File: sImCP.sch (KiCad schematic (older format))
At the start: 79 parts, among them J1 AVR-ISP-6, SW1 RESET, SW2 BOOT, U1 ATmega328P-AU, Y1 16MHz

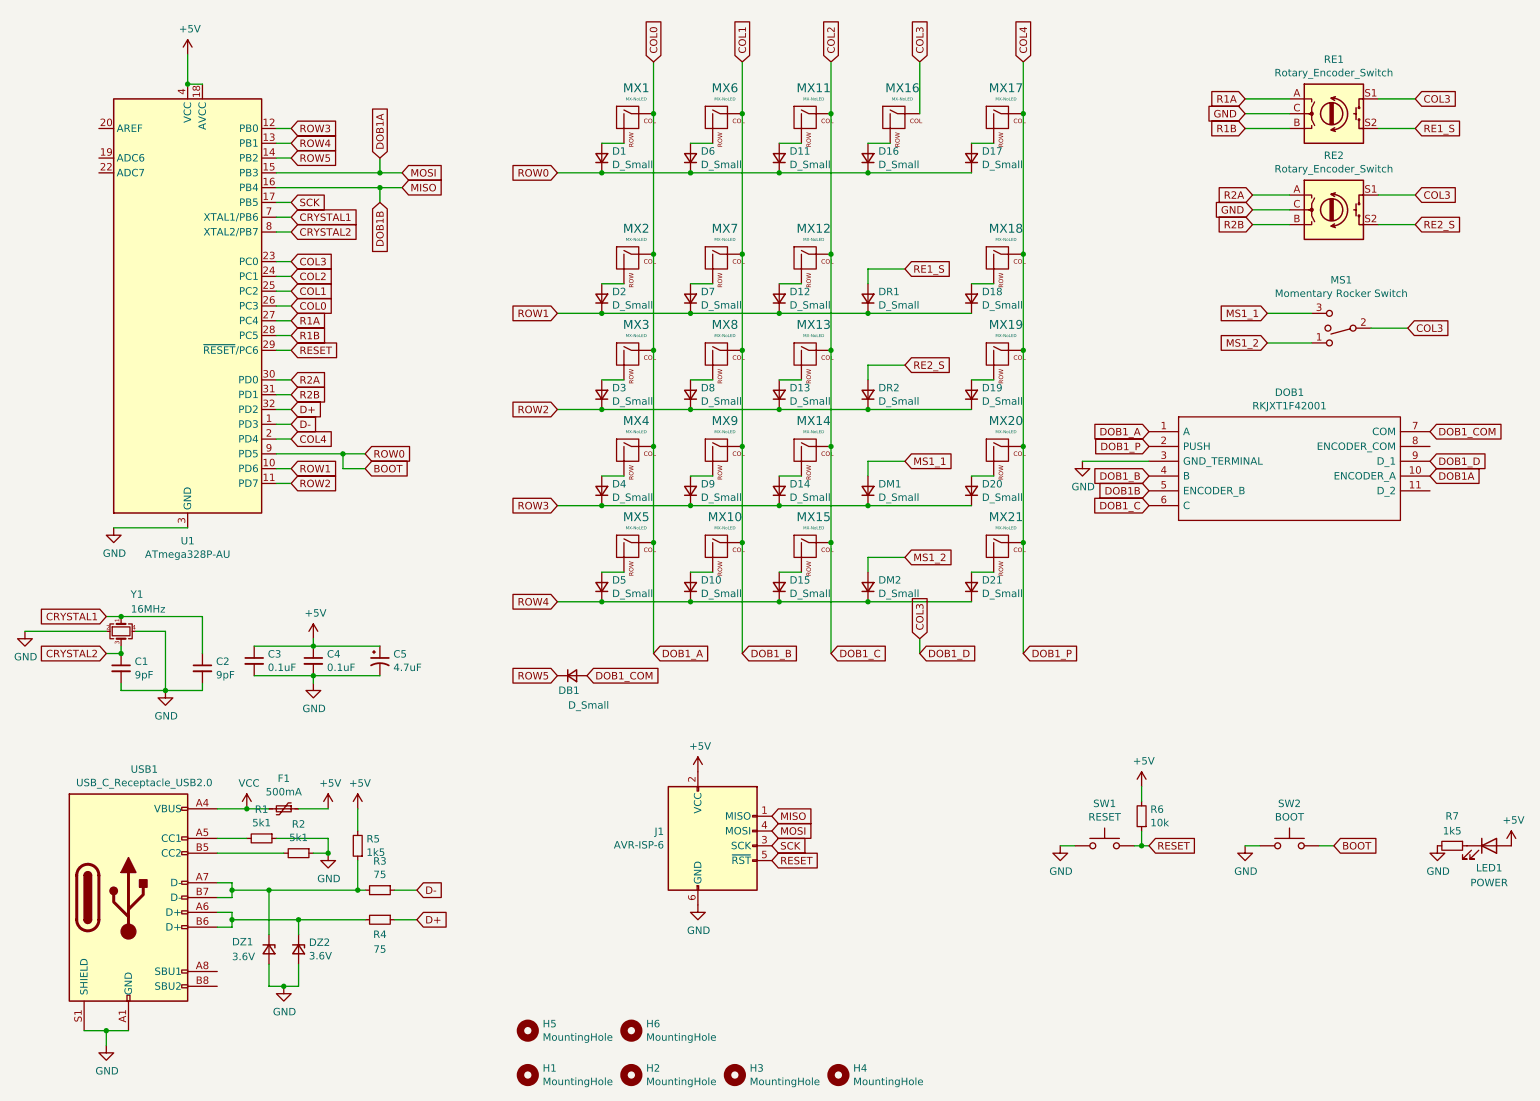
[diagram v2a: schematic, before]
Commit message: changed wiring to encoders sharing pins
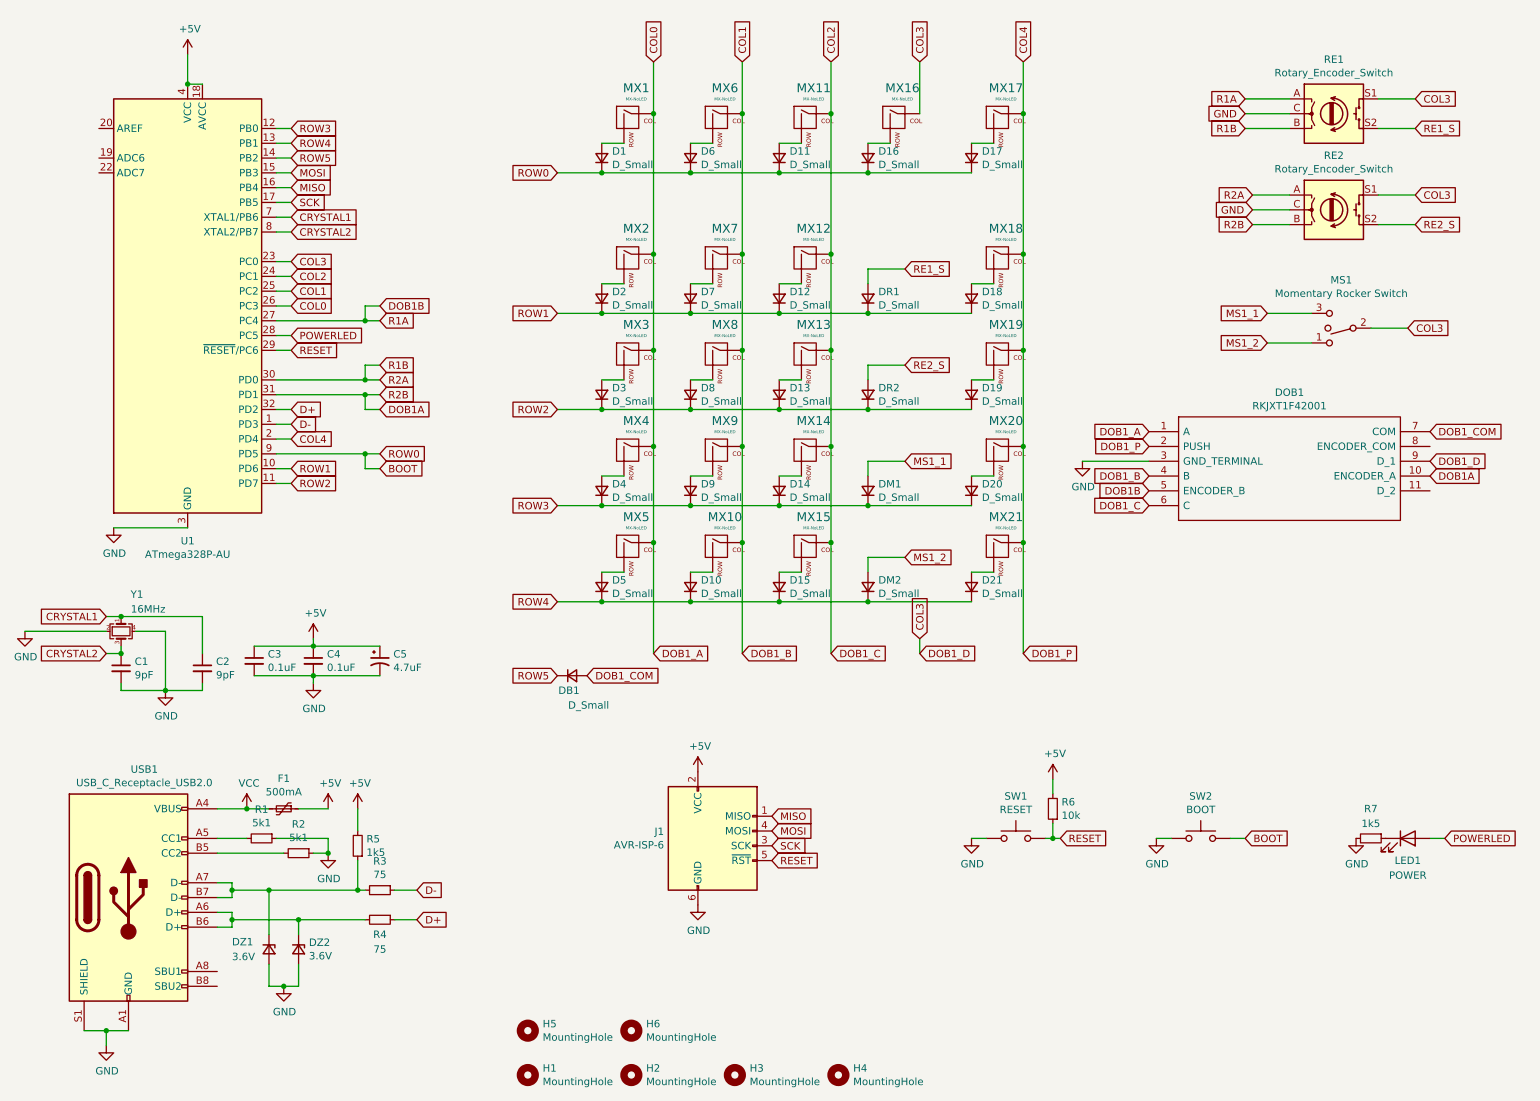
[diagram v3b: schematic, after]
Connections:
- net R1A is gone; now on net DOB1B: RE1.A, U1.27 (PC4)
- net R2A is gone; now on net R1B: RE2.A, U1.30 (PD0)
- net R2B is gone; now on net DOB1A: RE2.B, U1.31 (PD1)
- net +5V: no longer LED1.2 (A)
- net DOB1A: no longer J1.4 (MOSI), U1.15 (PB3)
- net DOB1B: no longer J1.1 (MISO), U1.16 (PB4)
- net R1B: no longer U1.28 (PC5)
- new net MISO: J1.1 (MISO), U1.16 (PB4)
- new net MOSI: J1.4 (MOSI), U1.15 (PB3)
- new net POWERLED: LED1.2 (A), U1.28 (PC5)
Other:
- moved on the sheet: LED1, R6, R7, SW1, SW2
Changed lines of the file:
@@
 Wire Wire Line
 	2550 2700 2450 2700
-Text GLabel 2550 1700 2    50   Input ~ 0
-SCK
-Text GLabel 3300 1500 2    50   Input ~ 0
+Text GLabel 2550 1500 2    50   Input ~ 0
 MOSI
-Text GLabel 3300 1600 2    50   Input ~ 0
+Text GLabel 2550 1600 2    50   Input ~ 0
 MISO
 Wire Wire Line
@@
 L power:GND #PWR0115
 U 1 1 60BC55AB
-P 7750 6050
-F 0 "#PWR0115" H 7750 5800 50  0001 C CNN
-F 1 "GND" H 7755 5877 50  0000 C CNN
-F 2 "" H 7750 6050 50  0001 C CNN
-F 3 "" H 7750 6050 50  0001 C CNN
-	1    7750 6050
+P 7150 6000
+F 0 "#PWR0115" H 7150 5750 50  0001 C CNN
+F 1 "GND" H 7155 5827 50  0000 C CNN
+F 2 "" H 7150 6000 50  0001 C CNN
+F 3 "" H 7150 6000 50  0001 C CNN
+	1    7150 6000
 	1    0    0    -1
 $EndComp
@@
 L Switch:SW_Push SW1
 U 1 1 60BC6C6D
-P 8050 6050
-F 0 "SW1" H 8050 6335 50  0000 C CNN
-F 1 "RESET" H 8050 6244 50  0000 C CNN
-F 2 "Connector_PinHeader_1.27mm:PinHeader_1x02_P1.27mm_Vertical" H 8050 6250 50  0001 C CNN
-F 3 "~" H 8050 6250 50  0001 C CNN
-	1    8050 6050
-	1    0    0    -1
-$EndComp
-Text GLabel 8350 6050 2    50   Input ~ 0
+P 7450 6000
+F 0 "SW1" H 7450 6285 50  0000 C CNN
+F 1 "RESET" H 7450 6194 50  0000 C CNN
+F 2 "Connector_PinHeader_1.27mm:PinHeader_1x02_P1.27mm_Vertical" H 7450 6200 50  0001 C CNN
+F 3 "~" H 7450 6200 50  0001 C CNN
+	1    7450 6000
+	1    0    0    -1
+$EndComp
+Text GLabel 7750 6000 2    50   Input ~ 0
 RESET
 $Comp
 L power:GND #PWR0116
 U 1 1 60BCAC21
-P 9000 6050
-F 0 "#PWR0116" H 9000 5800 50  0001 C CNN
-F 1 "GND" H 9005 5877 50  0000 C CNN
-F 2 "" H 9000 6050 50  0001 C CNN
-F 3 "" H 9000 6050 50  0001 C CNN
-	1    9000 6050
+P 8400 6000
+F 0 "#PWR0116" H 8400 5750 50  0001 C CNN
+F 1 "GND" H 8405 5827 50  0000 C CNN
+F 2 "" H 8400 6000 50  0001 C CNN
+F 3 "" H 8400 6000 50  0001 C CNN
+	1    8400 6000
 	1    0    0    -1
 $EndComp
@@
 L Switch:SW_Push SW2
 U 1 1 60BCAC27
-P 9300 6050
-F 0 "SW2" H 9300 6335 50  0000 C CNN
-F 1 "BOOT" H 9300 6244 50  0000 C CNN
-F 2 "Connector_PinHeader_1.27mm:PinHeader_1x02_P1.27mm_Vertical" H 9300 6250 50  0001 C CNN
-F 3 "~" H 9300 6250 50  0001 C CNN
-	1    9300 6050
-	1    0    0    -1
-$EndComp
-Text GLabel 9600 6050 2    50   Input ~ 0
+P 8700 6000
+F 0 "SW2" H 8700 6285 50  0000 C CNN
+F 1 "BOOT" H 8700 6194 50  0000 C CNN
+F 2 "Connector_PinHeader_1.27mm:PinHeader_1x02_P1.27mm_Vertical" H 8700 6200 50  0001 C CNN
+F 3 "~" H 8700 6200 50  0001 C CNN
+	1    8700 6000
+	1    0    0    -1
+$EndComp
+Text GLabel 9000 6000 2    50   Input ~ 0
 BOOT
 Wire Wire Line
-	9500 6050 9600 6050
-Wire Wire Line
-	9100 6050 9000 6050
-Wire Wire Line
-	7750 6050 7850 6050
-Wire Wire Line
-	8250 6050 8300 6050
+	8900 6000 9000 6000
+Wire Wire Line
+	8500 6000 8400 6000
+Wire Wire Line
+	7150 6000 7250 6000
+Wire Wire Line
+	7650 6000 7700 6000
 $Comp
 L Device:R_Small R6
 U 1 1 60BF3441
-P 8300 5850
-F 0 "R6" H 8241 5804 50  0000 R CNN
-F 1 "10k" H 8241 5895 50  0000 R CNN
-F 2 "Resistor_SMD:R_0603_1608Metric" H 8300 5850 50  0001 C CNN
-F 3 "~" H 8300 5850 50  0001 C CNN
-F 4 "C25804" H 8300 5850 50  0001 C CNN "LCSC"
-	1    8300 5850
+P 7700 5800
+F 0 "R6" H 7641 5754 50  0000 R CNN
+F 1 "10k" H 7641 5845 50  0000 R CNN
+F 2 "Resistor_SMD:R_0603_1608Metric" H 7700 5800 50  0001 C CNN
+F 3 "~" H 7700 5800 50  0001 C CNN
+F 4 "C25804" H 7700 5800 50  0001 C CNN "LCSC"
+	1    7700 5800
 	-1   0    0    1
 $EndComp
@@
 L power:+5V #PWR0117
 U 1 1 60BF4466
-P 8300 5650
-F 0 "#PWR0117" H 8300 5500 50  0001 C CNN
-F 1 "+5V" H 8315 5823 50  0000 C CNN
-F 2 "" H 8300 5650 50  0001 C CNN
-F 3 "" H 8300 5650 50  0001 C CNN
-	1    8300 5650
-	1    0    0    -1
-$EndComp
-Wire Wire Line
-	8300 5650 8300 5750
-Wire Wire Line
-	8300 5950 8300 6050
-Connection ~ 8300 6050
-Wire Wire Line
-	8300 6050 8350 6050
+P 7700 5600
+F 0 "#PWR0117" H 7700 5450 50  0001 C CNN
+F 1 "+5V" H 7715 5773 50  0000 C CNN
+F 2 "" H 7700 5600 50  0001 C CNN
+F 3 "" H 7700 5600 50  0001 C CNN
+	1    7700 5600
+	1    0    0    -1
+$EndComp
+Wire Wire Line
+	7700 5600 7700 5700
+Wire Wire Line
+	7700 5900 7700 6000
+Connection ~ 7700 6000
+Wire Wire Line
+	7700 6000 7750 6000
 $Comp
 L Device:D_Small D17
@@
 L power:GND #PWR0118
 U 1 1 60CCE9F8
-P 10300 6050
-F 0 "#PWR0118" H 10300 5800 50  0001 C CNN
-F 1 "GND" H 10305 5877 50  0000 C CNN
-F 2 "" H 10300 6050 50  0001 C CNN
-F 3 "" H 10300 6050 50  0001 C CNN
-	1    10300 6050
+P 9750 6000
+F 0 "#PWR0118" H 9750 5750 50  0001 C CNN
+F 1 "GND" H 9755 5827 50  0000 C CNN
+F 2 "" H 9750 6000 50  0001 C CNN
+F 3 "" H 9750 6000 50  0001 C CNN
+	1    9750 6000
 	1    0    0    -1
 $EndComp
@@
 L Device:R_Small R7
 U 1 1 60CD08C2
-P 10400 6050
-F 0 "R7" V 10200 6050 50  0000 C CNN
-F 1 "1k5" V 10300 6050 50  0000 C CNN
-F 2 "Resistor_SMD:R_0603_1608Metric" H 10400 6050 50  0001 C CNN
-F 3 "~" H 10400 6050 50  0001 C CNN
-F 4 "C22843" H 10400 6050 50  0001 C CNN "LCSC"
-	1    10400 6050
+P 9850 6000
+F 0 "R7" V 9650 6000 50  0000 C CNN
+F 1 "1k5" V 9750 6000 50  0000 C CNN
+F 2 "Resistor_SMD:R_0603_1608Metric" H 9850 6000 50  0001 C CNN
+F 3 "~" H 9850 6000 50  0001 C CNN
+F 4 "C22843" H 9850 6000 50  0001 C CNN "LCSC"
+	1    9850 6000
 	0    1    1    0
 $EndComp
@@
 L Device:LED LED1
 U 1 1 60CD343C
-P 10650 6050
-F 0 "LED1" H 10650 5900 50  0000 C CNN
-F 1 "POWER" H 10650 5800 50  0000 C CNN
-F 2 "LED_SMD:LED_0805_2012Metric" H 10650 6050 50  0001 C CNN
-F 3 "~" H 10650 6050 50  0001 C CNN
-F 4 " 	C205442" H 10650 6050 50  0001 C CNN "LCSC"
-	1    10650 6050
-	1    0    0    -1
-$EndComp
-$Comp
-L power:+5V #PWR0119
-U 1 1 60CD4FF3
-P 10800 6050
-F 0 "#PWR0119" H 10800 5900 50  0001 C CNN
-F 1 "+5V" H 10815 6223 50  0000 C CNN
-F 2 "" H 10800 6050 50  0001 C CNN
-F 3 "" H 10800 6050 50  0001 C CNN
-	1    10800 6050
+P 10100 6000
+F 0 "LED1" H 10100 5850 50  0000 C CNN
+F 1 "POWER" H 10100 5750 50  0000 C CNN
+F 2 "LED_SMD:LED_0805_2012Metric" H 10100 6000 50  0001 C CNN
+F 3 "~" H 10100 6000 50  0001 C CNN
+F 4 " 	C205442" H 10100 6000 50  0001 C CNN "LCSC"
+	1    10100 6000
 	1    0    0    -1
 $EndComp
@@
 	7500 4000 7500 4750
 Connection ~ 7500 4000
-Text GLabel 3050 3500 2    50   Input ~ 0
+Text GLabel 3150 3500 2    50   Input ~ 0
 BOOT
-Text GLabel 3050 3400 2    50   Input ~ 0
+Text GLabel 3150 3400 2    50   Input ~ 0
 ROW0
-Wire Wire Line
-	2900 3400 2900 3500
-Wire Wire Line
-	2900 3500 3050 3500
-Wire Wire Line
-	2900 3400 3050 3400
 Text GLabel 2550 3500 2    50   Input ~ 0
 ROW1
@@
 Wire Wire Line
 	2550 3600 2450 3600
-Wire Wire Line
-	2900 3400 2450 3400
-Connection ~ 2900 3400
 Text GLabel 2550 3300 2    50   Input ~ 0
 COL4
@@
 Wire Wire Line
 	2450 2400 2550 2400
-Text GLabel 2550 2500 2    50   Input ~ 0
+Text GLabel 3150 2500 2    50   Input ~ 0
 R1A
-Text GLabel 2550 2600 2    50   Input ~ 0
+Text GLabel 3150 2800 2    50   Input ~ 0
 R1B
-Text GLabel 2550 2900 2    50   Input ~ 0
+Text GLabel 3150 2900 2    50   Input ~ 0
 R2A
-Text GLabel 2550 3000 2    50   Input ~ 0
+Text GLabel 3150 3000 2    50   Input ~ 0
 R2B
 Wire Wire Line
-	2550 3000 2450 3000
-Wire Wire Line
-	2450 2900 2550 2900
-Wire Wire Line
 	2550 2600 2450 2600
-Wire Wire Line
-	2450 2500 2550 2500
-Wire Wire Line
-	2450 1500 3150 1500
-Wire Wire Line
-	2450 1600 3150 1600
-Text GLabel 3150 1400 1    50   Input ~ 0
+Text GLabel 3150 3100 2    50   Input ~ 0
 DOB1A
-Wire Wire Line
-	3150 1700 3150 1600
-Connection ~ 3150 1600
-Wire Wire Line
-	3150 1600 3300 1600
-Wire Wire Line
-	3150 1500 3150 1400
-Connection ~ 3150 1500
-Wire Wire Line
-	3150 1500 3300 1500
-Text GLabel 3150 1700 3    50   Input ~ 0
+Text GLabel 3150 2400 2    50   Input ~ 0
 DOB1B
 $Comp
@@
 	1    0    0    -1
 $EndComp
+Wire Wire Line
+	2450 1600 2550 1600
+Text GLabel 2550 1700 2    50   Input ~ 0
+SCK
+Wire Wire Line
+	2550 1500 2450 1500
+Wire Wire Line
+	3150 3100 3050 3100
+Wire Wire Line
+	3050 3100 3050 3000
+Wire Wire Line
+	3050 3000 3150 3000
+Wire Wire Line
+	3150 2900 3050 2900
+Wire Wire Line
+	3050 2900 3050 2800
+Wire Wire Line
+	3050 2800 3150 2800
+Wire Wire Line
+	3050 2500 3050 2400
+Wire Wire Line
+	3050 2400 3150 2400
+Wire Wire Line
+	3050 2500 3150 2500
+Wire Wire Line
+	2450 2500 3050 2500
+Connection ~ 3050 2500
+Wire Wire Line
+	2450 2900 3050 2900
+Connection ~ 3050 2900
+Wire Wire Line
+	2450 3000 3050 3000
+Connection ~ 3050 3000
+Text GLabel 10350 6000 2    50   Input ~ 0
+POWERLED
+Wire Wire Line
+	10350 6000 10250 6000
+Text GLabel 2550 2600 2    50   Input ~ 0
+POWERLED
+Wire Wire Line
+	3150 3400 3050 3400
+Wire Wire Line
+	3050 3400 3050 3500
+Wire Wire Line
+	3050 3500 3150 3500
+Wire Wire Line
+	3050 3400 2450 3400
+Connection ~ 3050 3400
 $EndSCHEMATC
